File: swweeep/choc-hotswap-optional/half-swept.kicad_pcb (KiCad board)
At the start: 2 copper layers, 113.3 x 89.7 mm, 35 parts, among them J1 JST-BATTERY, SW1 SW_Push, SW10 SW_Push, SW11 SW_Push, SW12 SW_Push, SW13 SW_DPDT, SW14 SW_Push, SW15 SW_Push, SW16 SW_Push, SW17 SW_Push, SW18 SW_Push, SW2 SW_Push, SW20 SW_Push, SW21 SW_Push, SW3 SW_Push, SW4 SW_Push, SW5 SW_Push, SW6 SW_Push, SW7 SW_DPDT, SW8 SW_Push, SW9 SW_Push, U1 nice_nano

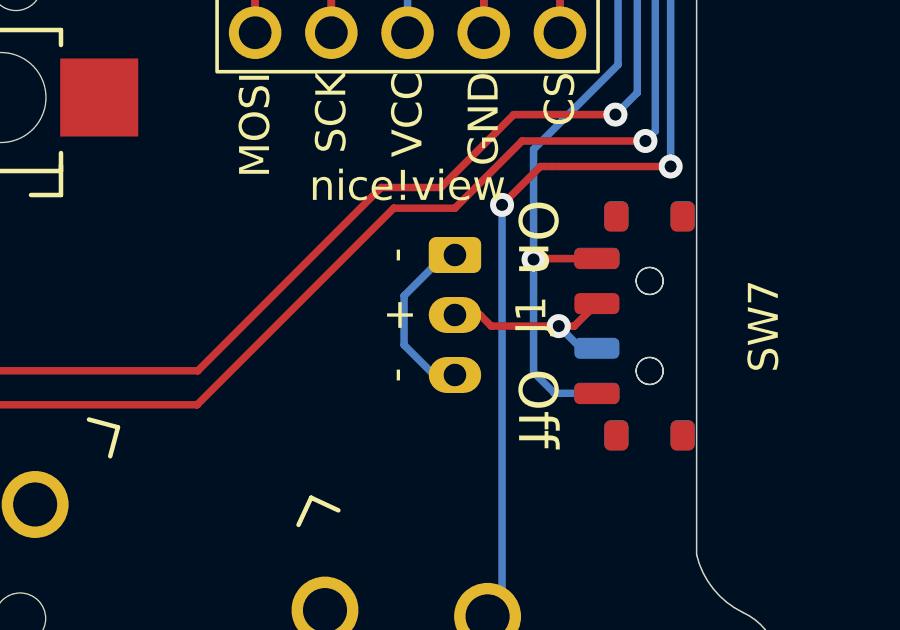
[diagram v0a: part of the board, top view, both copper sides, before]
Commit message: updated footprints to have user.drawings for easier svg exports
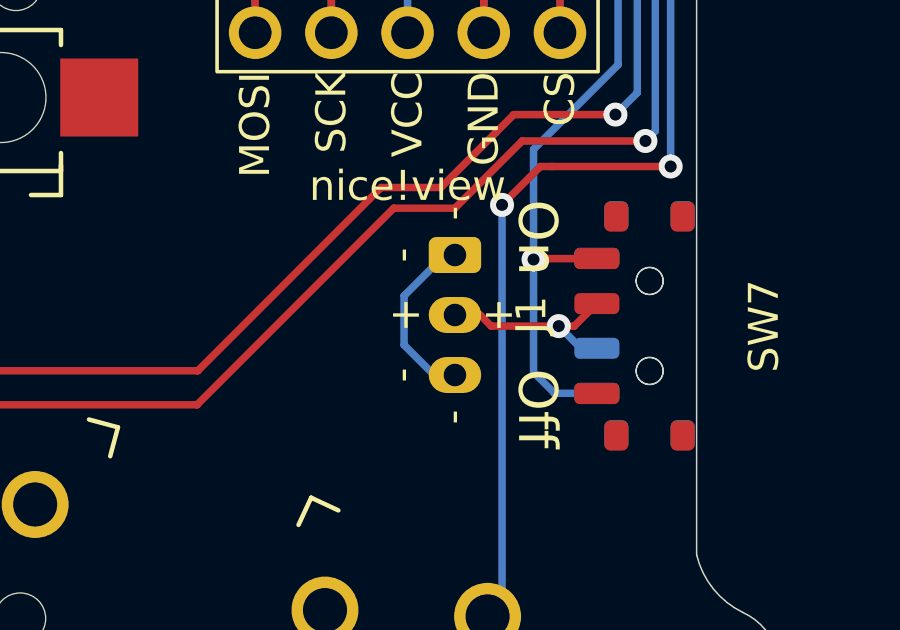
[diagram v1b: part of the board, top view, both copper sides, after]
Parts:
- J1: footprint Connector_JST:JST_PH_S3B-PH-K_1x03_P2.00mm_Horizontal -> fingerpunch:JST_PH_S3B-PH-K-keyboard

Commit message: fixed unconnected battery ground and updated readme with pics
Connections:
- J1 pad 1: GND -> gnd
- J1 pad 3: GND -> gnd
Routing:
- net GND: track 6.00 -> 0.00 mm
- net gnd: track 31.6 -> 32.6 mm

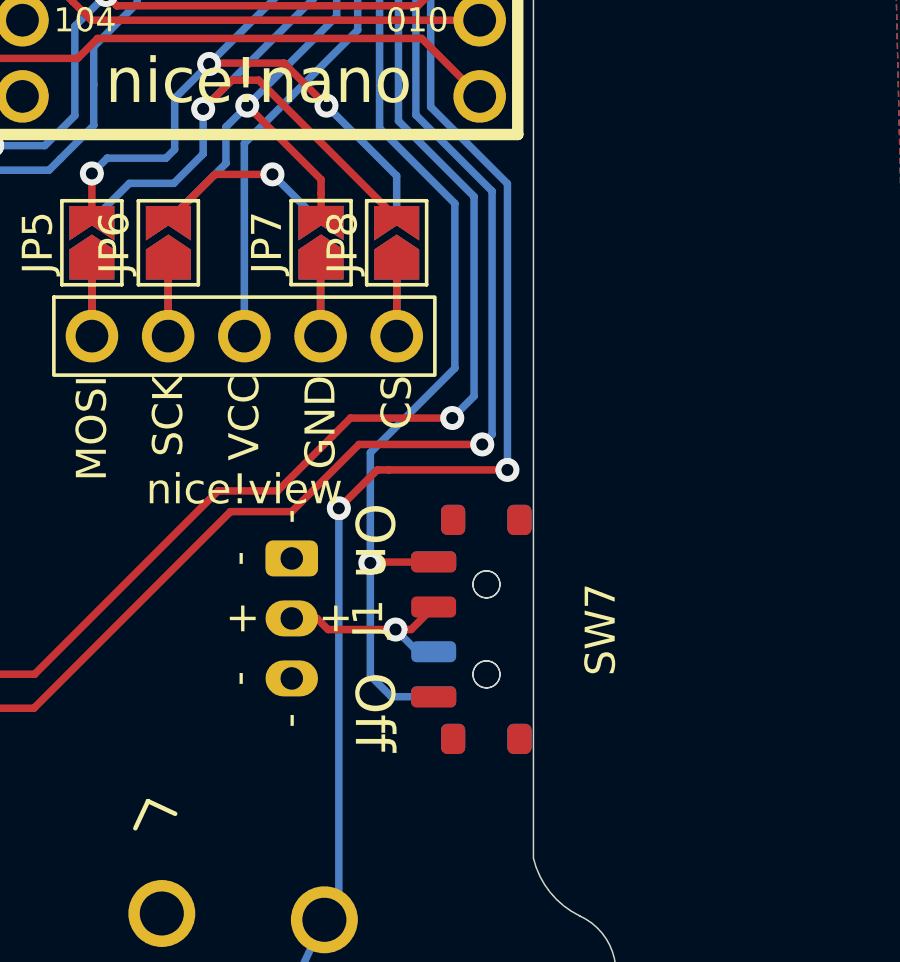
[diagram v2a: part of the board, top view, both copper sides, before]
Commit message: replaced on off switch, from MSK12C02 to OS102011MA1QN1
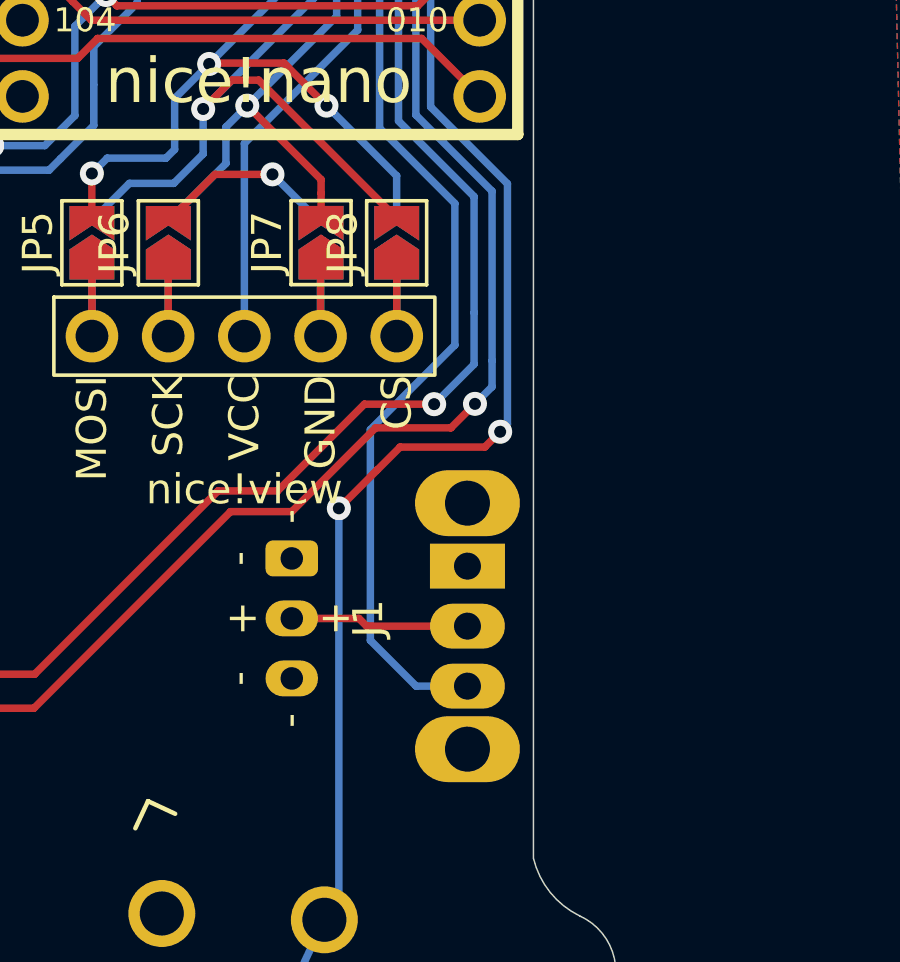
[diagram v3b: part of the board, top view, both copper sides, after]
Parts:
- removed SW13: SW_DPDT, fingerpunch:MSK-12C02
- SW7: footprint fingerpunch:MSK-12C02 -> fingerpunch:SW_CuK_OS102011MA1QN1_SPDT_Angled; moved to B.Cu
- moved SW7 2.21 mm to (120.6, 73.6)
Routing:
- net raw: track 57.2 -> 55.4 mm, vias 2 -> 1
- net gnd: track 32.6 -> 31.6 mm
- net Switch17: track 77.6 -> 76.7 mm
- net Switch16: track 67.4 -> 66.5 mm
- net Net-(J1-Pad2): track 6.77 -> 5.96 mm, vias 1 -> 0
- net Switch18: track 99.8 -> 99.2 mm
